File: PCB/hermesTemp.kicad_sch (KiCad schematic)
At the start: 18 parts, among them U1 N069-9616TSWPG02-H14, U2 AHT20, U3 STM32F103C8T6

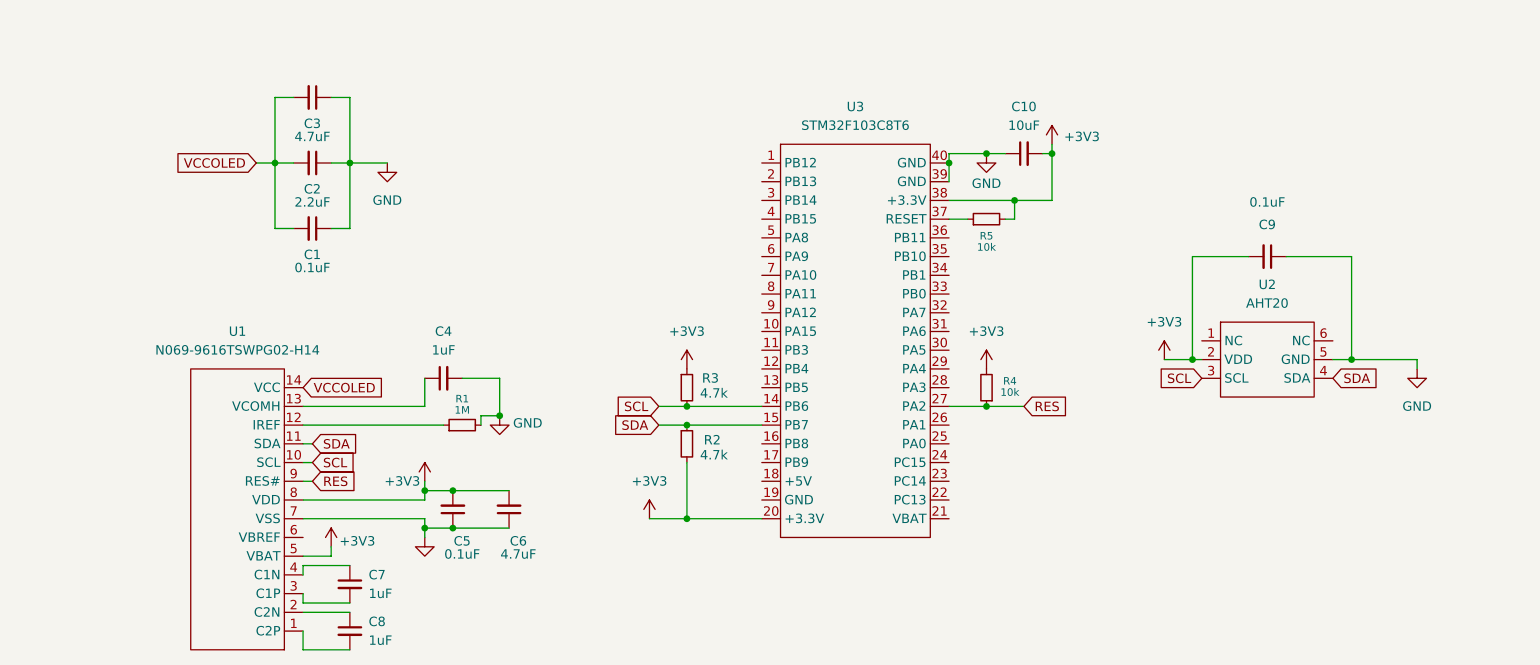
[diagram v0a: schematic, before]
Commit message: Update based on reviewer feedback.
Switched to XIAO RP2040 (dropped STM32 + PCBA for MCU/OLED) to simplify design and reduce cost. Increased project complexity by adding STK8328 accelerometer and AGR10 pressure sensor alongside AHT20. Updated schematic and firmware to support multi-sensor setup (I2C + analog) and display all data on OLED.
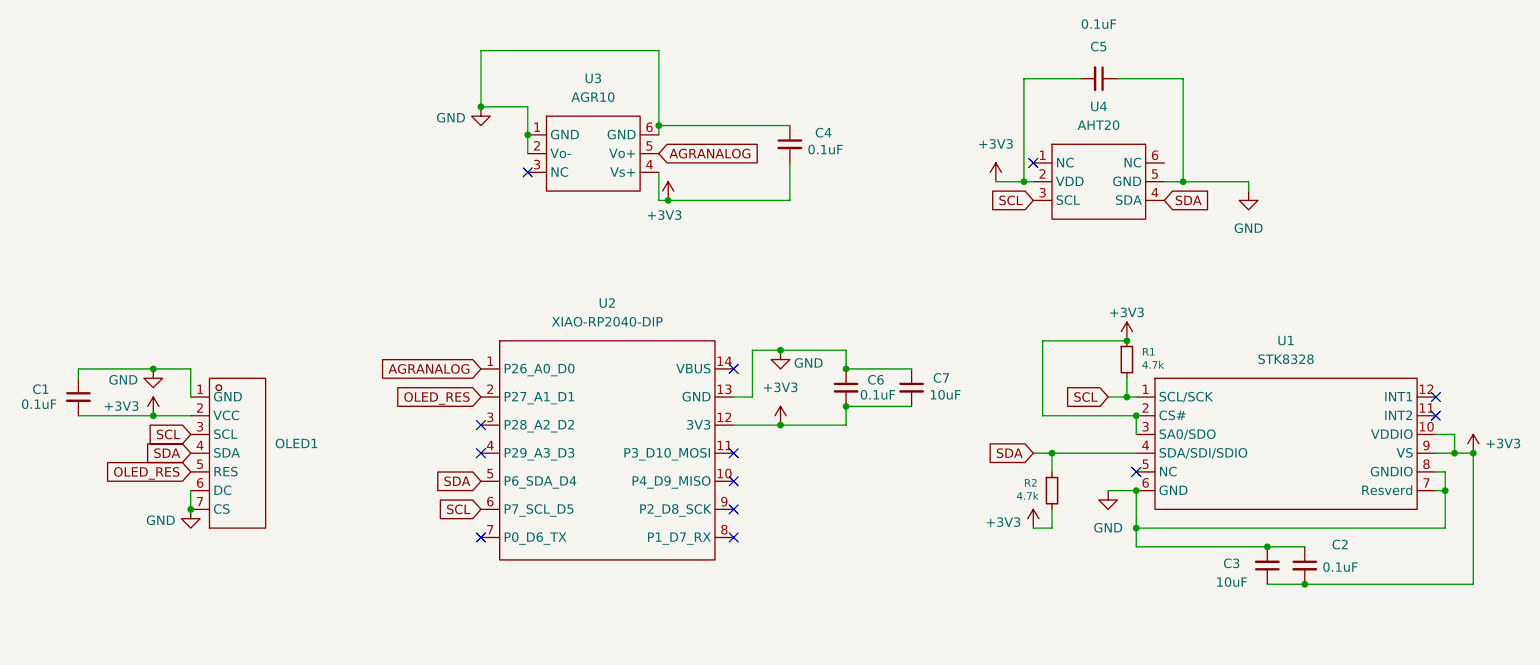
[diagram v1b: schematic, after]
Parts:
- removed C10: 10uF, Capacitor_SMD:C_0603_1608Metric, symbol Device:C_Small
- removed C5: 0.1uF, Capacitor_SMD:C_0603_1608Metric, symbol Device:C_Small
- removed C8: 1uF, Capacitor_SMD:C_0603_1608Metric, symbol Device:C_Small
- removed R3: 4.7k, Resistor_SMD:R_0603_1608Metric, symbol Device:R_Small
- removed R4, R5: 10k, Resistor_SMD:R_0603_1608Metric, symbol Device:R_Small
- removed U1: N069-9616TSWPG02-H14, hermesExtraFoot:LCD-SMD_N069-9616TSWPG02-H14, symbol hermesExtraFoot:N069-9616TSWPG02-H14
- removed U3: STM32F103C8T6, hermesExtraFoot:STM32F103C8T6, symbol hermesExtraFoot:LCKFB-DKX-STM32F103C8T6
- added OLED1: ~, hermesExtraFoot:OLED-TH_HS96L01W4S03, symbol hermesExtraFoot:HS96L01W4S03
- added U1: STK8328, hermesExtraFoot:VLGA-12_L2.0-W2.0-P0.50-BL, symbol hermesExtraFoot:STK8328-C
- added U2: XIAO-RP2040-DIP, hermesExtraFoot:XIAO-RP2040-DIP, symbol XIAO-RP2040-DIP:XIAO-RP2040-DIP
- added U3: AGR10, hermesExtraFoot:KEY-SMD_6P-L7.0-W7.0-P2.54-LS10.6, symbol hermesExtraFoot:AGR10
- C2: value 2.2uF -> 0.1uF
- C3: value 4.7uF -> 10uF; footprint Capacitor_SMD:C_0603_1608Metric -> Capacitor_SMD:C_0805_2012Metric
- C4: value 1uF -> 0.1uF
- C6: value 4.7uF -> 0.1uF
- C7: value 1uF -> 10uF; footprint Capacitor_SMD:C_0603_1608Metric -> Capacitor_SMD:C_0805_2012Metric
- R1: value 1M -> 4.7k
- renumbered C9 to C5, U2 to U4
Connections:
- net +3V3: now also C1.2, C2.2, C3.1, C4.2, C7.2, R1.1, OLED1.2 (VCC), U1.10 (VDDIO), U1.2 (CS#), U1.3 (SA0/SDO), U1.9 (VS), U2.12 (3V3), U3.4 (Vs+)
- net GND: now also C3.2, C4.1, C7.1, OLED1.1 (GND), OLED1.6 (DC), OLED1.7 (CS), U1.6 (GND), U1.7 (Resverd), U1.8 (GNDIO), U2.13 (GND), U3.1 (GND), U3.2 (Vo-), U3.6 (GND); no longer C3.1, C4.2, R1.2
- net SCL: now also R1.2, OLED1.3 (SCL), U1.1 (SCL/SCK), U2.6 (P7_SCL_D5)
- net SDA: now also OLED1.4 (SDA), U1.4 (SDA/SDI/SDIO), U2.5 (P6_SDA_D4)
- removed net VCCOLED: C1.2, C2.2, C3.2
- new net AGRANALOG: U2.1 (P26_A0_D0), U3.5 (Vo+)
- new net OLED_RES: OLED1.5 (RES), U2.2 (P27_A1_D1)
- no-connect marks 0 -> 13
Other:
- moved on the sheet: C5, U4

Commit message: Build review update
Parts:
- removed U2: XIAO-RP2040-DIP, hermesExtraFoot:XIAO-RP2040-DIP, symbol XIAO-RP2040-DIP:XIAO-RP2040-DIP
- removed U3: AGR10, hermesExtraFoot:KEY-SMD_6P-L7.0-W7.0-P2.54-LS10.6, symbol hermesExtraFoot:AGR10
- added U2: RP2040-ZERO, hermesExtraFoot:MODULE_RP2040-ZERO, symbol hermesExtraFoot:RP2040-ZERO
- added U3: ~, hermesExtraFoot:LGA-8_L3.8-W3.6-P0.90-TL_WF183D, symbol hermesExtraFoot:WF183DE 15BA L8N T&R
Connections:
- net +3V3: now also U2.21 (3V3), U3.3 (VDD)
- net AGRANALOG: now also U2.17 (GP26)
- net GND: now also U2.22 (GND), U3.2 (GND)
- net OLED_RES: now also U2.7 (GP6)
- net SCL: now also U2.6 (GP5), U3.1 (SCL)
- net SDA: now also U2.5 (GP4), U3.8 (SDA)
- no-connect marks 13 -> 4
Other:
- moved on the sheet: C4, C6, C7
